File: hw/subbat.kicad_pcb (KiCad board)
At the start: 2 copper layers, 100 x 100 mm, 232 parts, among them J1 Conn_01x02, J10 Conn_01x06_Male, J11 USB_Ax2, J12 USB_Ax2, J13 USB_Ax2, J14 Conn_01x02, J15 Conn_01x04_Male, J16 Conn_01x06_Male, J17 Conn_01x06_Male, J18 Conn_01x02, J19 USB_B_Micro, J2 Conn_01x02, J20 Conn_02x08_Odd_Even, J21 Conn_01x02, J22 Conn_01x02, J24 Conn_01x02, J3 Conn_01x02, J4 Conn_01x02, J5 Conn_01x02, J6 Conn_01x02, J7 Conn_01x06_Male, J8 Conn_01x02, J9 USB_Ax2, Q1 Q_NPN_BEC, Q10 Q_NPN_BEC, Q11 AOD403, Q12 AOD403, Q13 Q_NPN_BEC, Q14 AOD403, Q15 Q_NPN_BEC, Q16 Q_Photo_NPN_EC, Q17 Q_NPN_BEC, Q18 Q_PNP_BEC, Q2 Q_PMOS_GSD, Q9 AOD403, SW1 SW_Push, SW2 SW_Push, SW3 SW_Push, SW4 SW_SPDT_WITH_SHIELD, SW5 SW_SPDT_WITH_SHIELD, U1 ATMEGA328P-AU, U10 P82B715, U11 TPS54202, U12 L7803, U13 TPS54202, U2 L7803, U3 ATTINY2313-20SU, U4 ATTINY13A-SSU, U5 LT6105, U6 LT6105, U7 LT6105, U8 LT6105, U9 LM393

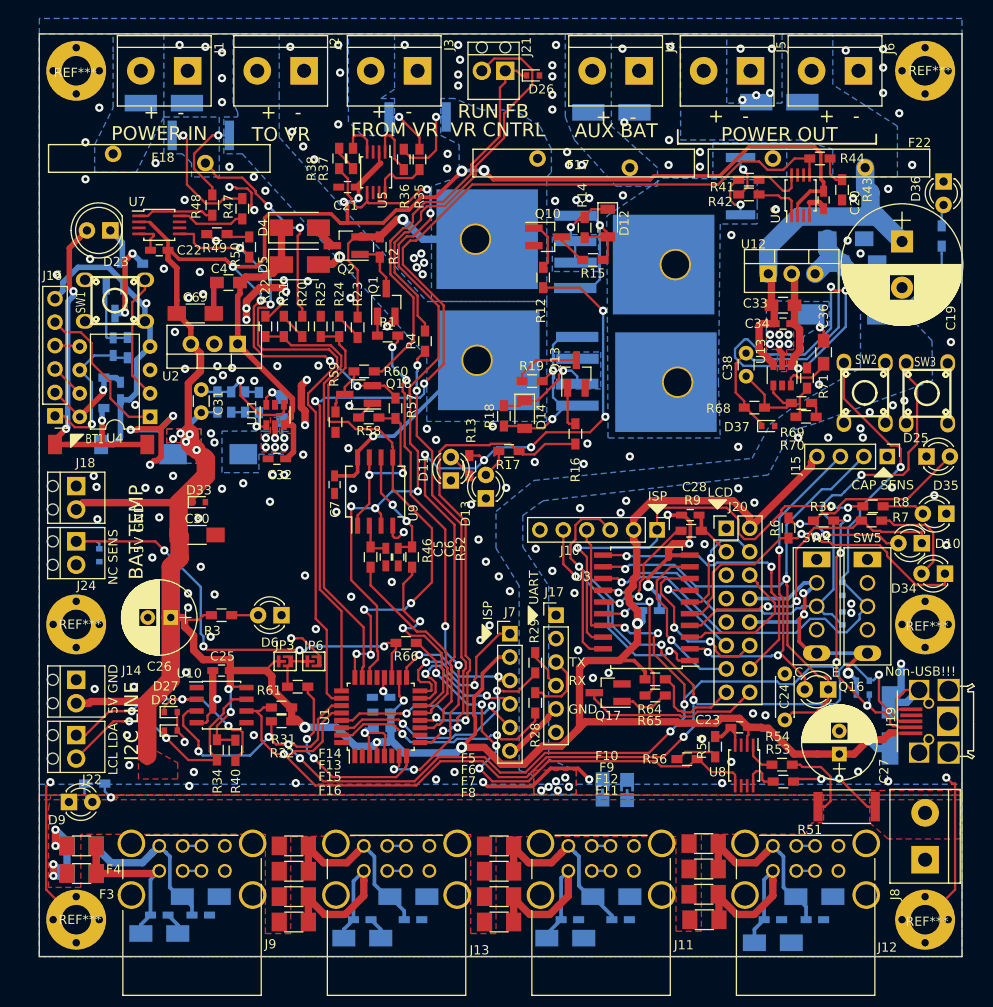
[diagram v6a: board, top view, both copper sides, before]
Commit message: To use RJ45 connector to join Main/Sub MCUs; DRC clear
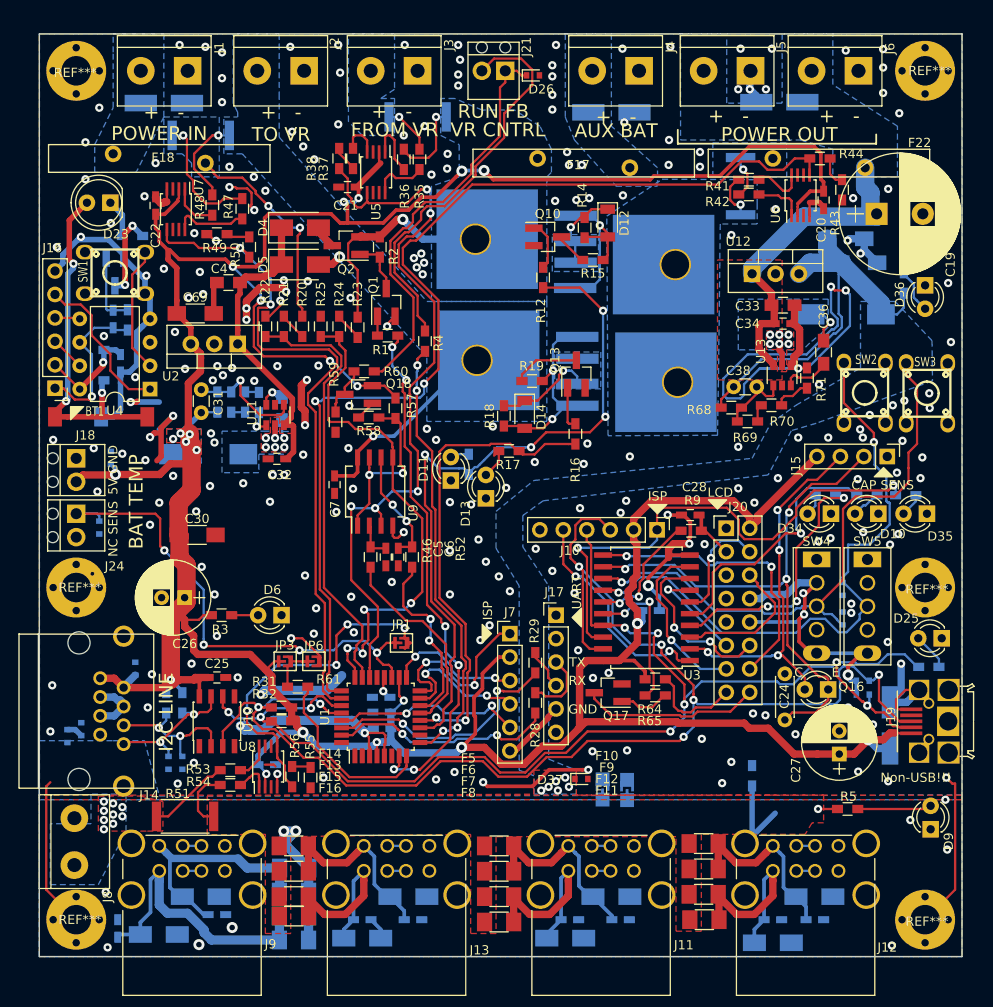
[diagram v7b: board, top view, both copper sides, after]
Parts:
- removed D33: ESD5Z5.0T1G, Diodes_SMD:D_SOD-523
- removed J22: Conn_01x02, components:TerminalBlock_2_P_2.54mm
- added D38: ESD5Z5.0T1G, Diodes_SMD:D_SOD-523, B.Cu at (30.4, 88.8)
- added D39: ESD5Z5.0T1G, Diodes_SMD:D_SOD-523, B.Cu at (23.1, 96.1)
- added D40: ESD5Z5.0T1G, Diodes_SMD:D_SOD-523, B.Cu at (24.6, 95.3)
- added D41: ESD5Z5.0T1G, Diodes_SMD:D_SOD-523, B.Cu at (27.8, 66.0)
- added JP1: Jumper_NO_Small, components:SolderJumper, F.Cu at (59.2, 86.0)
- C23, D27, D28, F3, F4, R13, R30, R34, R40, R6, R7, R8: moved to B.Cu
- C26: value CP1_Small -> 100u
- J14: value Conn_01x02 -> RJ45; footprint components:TerminalBlock_2_P_2.54mm -> components:RJ45_8_Neltron-7810
- R5: moved to F.Cu
- R66: value 0R -> 470k; moved to B.Cu
- moved D9 93.4 mm to (116.6, 106.2), turned to 90 degrees
- moved J8 92.3 mm to (23.8, 105.0), turned to 270 degrees
- moved R5 81.6 mm to (107.6, 104.0), turned to 0 degrees
- moved R51 71.7 mm to (35.8, 104.8), turned to 180 degrees
- moved R53 60.0 mm to (40.7, 99.8), turned to 0 degrees
- moved R54 59.8 mm to (40.7, 101.4), turned to 0 degrees
- moved U8 51.6 mm to (44.8, 99.4), turned to 90 degrees
- moved C23 51.4 mm to (44.6, 99.2), turned to 0 degrees
- moved R55 44.0 mm to (49.4, 100.6), turned to 270 degrees
- moved D37 43.3 mm to (78.8, 100.8)
- moved R56 42.8 mm to (47.4, 100.5), turned to 270 degrees
- moved R66 40.2 mm to (97.2, 100.4), turned to 90 degrees
- moved F4 25.2 mm to (47.6, 118.2), turned to 0 degrees
- moved F3 23.5 mm to (47.6, 115.6), turned to 0 degrees
- moved F1 23.2 mm to (47.6, 110.4), turned to 0 degrees
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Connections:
- D10 pad 1: Net-(D10-Pad1) -> GND
- D34 pad 1: Net-(D34-Pad1) -> GND
- J14 pad 1: GND -> /SDA_L
- J14 pad 2: +5V -> GND
- R6 pad 1: Net-(D34-Pad1) -> Net-(R6-Pad1)
- R66 pad 1: /IUSB_SENS -> BUSGND
- R66 pad 2: /BAT_TEMP_SENS -> GND
- R7 pad 1: Net-(D10-Pad1) -> Net-(R7-Pad1)
- U10 pad 2: /SDA_L -> /SCL_L
- U10 pad 3: SDA -> SCL
- U10 pad 6: SCL -> SDA
- U10 pad 7: /SCL_L -> /SDA_L
- U3 pad 4: Net-(D10-Pad1) -> Net-(R7-Pad1)
- U3 pad 5: Net-(D34-Pad1) -> Net-(R6-Pad1)
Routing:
- net Net-(D34-Pad1): track 36.8 -> 0.00 mm, vias 2 -> 0
- net Net-(D10-Pad1): track 35.2 -> 0.00 mm, vias 2 -> 0
- net GND: track 299.8 -> 334.0 mm, vias 213 -> 239
- net Net-(R6-Pad1): track 0.00 -> 28.9 mm, vias 0 -> 1
- net Net-(R7-Pad1): track 0.00 -> 28.4 mm, vias 0 -> 3
- net SDA: track 156.3 -> 140.7 mm, vias 12 -> 9
- net Net-(C9-Pad1): track 17.6 -> 31.4 mm
- net Net-(D25-Pad2): track 17.9 -> 4.19 mm
- net /SDA_L: track 28.9 -> 15.6 mm, vias 3 -> 2
- net /SCL_L: track 29.7 -> 16.6 mm
- net /IUSB_SENS: track 50.6 -> 38.7 mm
- net BUSGND: track 6.67 -> 16.7 mm, vias 0 -> 8
- net Net-(D10-Pad2): track 13.0 -> 3.23 mm, vias 2 -> 0
- net VCOM: track 78.1 -> 69.1 mm, vias 11 -> 9
- net Net-(D34-Pad2): track 11.1 -> 2.35 mm
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- added copper zone on B.Cu, net /VBUS_COM_IN
- added copper zone on F.Cu, net /VOUT2
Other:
- board text removed: "LCL LDA"

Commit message: Added output cap soft start circuit; DRC clear
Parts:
- added C39: 1u, Capacitors_SMD:C_0603_HandSoldering, B.Cu at (26.7, 101.0)
- added C40: 1u, Capacitors_SMD:C_0603_HandSoldering, B.Cu at (58.6, 21.2)
- added C41: 1u, Capacitors_SMD:C_0603_HandSoldering, B.Cu at (46.0, 21.3)
- added C42: 1u, Capacitors_SMD:C_0603_HandSoldering, B.Cu at (82.4, 21.2)
- added C43: 1u, Capacitors_SMD:C_0603_HandSoldering, B.Cu at (33.4, 21.2)
- added C44: 1u, Capacitors_SMD:C_0603_HandSoldering, B.Cu at (100.3, 21.3)
- added C45: 1u, Capacitors_SMD:C_0603_HandSoldering, B.Cu at (118.2, 46.8)
- added Q3: TPH11006NL, components:TDSON-8-1_HandSoldering_mod, F.Cu at (116.5, 40.1)
- added R72: 1M, Resistors_SMD:R_0603_HandSoldering, B.Cu at (112.2, 83.4)
- added R73: 10k, Resistors_SMD:R_0603_HandSoldering, F.Cu at (61.8, 54.8)
- added R74: 10k, Resistors_SMD:R_0603_HandSoldering, F.Cu at (118.2, 34.0)
- added R75: 100k, Resistors_SMD:R_0603_HandSoldering, B.Cu at (118.7, 50.8)
- C19: value 1600u 50V -> 2200u 35V x 2; footprint Capacitors_ThroughHole:CP_Radial_D13.0mm_P5.00mm -> Capacitors_ThroughHole:CP_Radial_D5.0mm_P2.50mm
- R4, R60: value 1k -> 2.2k
- moved R12 2.42 mm to (76.5, 44.9)
- moved R4 2.40 mm to (61.8, 50.9)
- moved C21 2.35 mm to (53.9, 34.3), turned to 90 degrees
- moved R37 1.70 mm to (52.3, 33.5)
- moved R38 1.70 mm to (50.8, 33.5)
- moved Q13 1.64 mm to (78.0, 58.5)
- moved C19 0.51 mm to (110.2, 39.4)
- turned SW2 to 0 degrees
- turned SW3 to 0 degrees
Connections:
- C19 pad 2: GND -> /OUTCAP_N
- R23 pad 1: /VA -> /VA_G
- SW4 pad 4: GND -> Net-(R72-Pad1)
- SW4 pad 5: GND -> Net-(R72-Pad1)
- SW5 pad 4: GND -> Net-(R72-Pad1)
- SW5 pad 5: GND -> Net-(R72-Pad1)
- U1 pad 32: Net-(U1-Pad32) -> /OUTCAP_CHARGE
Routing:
- net /OUTCAP_CHARGE: track 0.00 -> 116.9 mm, vias 0 -> 5
- net Net-(R72-Pad1): track 0.00 -> 32.9 mm
- net GND: track 334.0 -> 350.8 mm, vias 239 -> 247
- net /OUTCAP_N: track 0.00 -> 12.5 mm
- net /VA_G: track 2.57 -> 12.2 mm
- net /VA: track 33.4 -> 24.4 mm
- net Net-(C45-Pad2): track 0.00 -> 7.13 mm, vias 0 -> 1
- net BUSGND: track 16.7 -> 21.8 mm
- net /WaterLevel/ALLOW_DISCHG: track 63.6 -> 59.0 mm, vias 1 -> 2
- net /WaterLevel/PREFER_DISCHG: track 67.9 -> 63.5 mm
- net /SW_VR: track 48.5 -> 52.0 mm
- net Net-(J21-Pad2): track 43.7 -> 41.3 mm
- net /CCCV_IN: track 5.51 -> 7.50 mm
- net Net-(Q13-Pad1): track 4.64 -> 3.07 mm
- net /ICHARGE_SENS: track 82.6 -> 84.1 mm
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- added copper zone on F.Cu, net /OUTCAP_N
